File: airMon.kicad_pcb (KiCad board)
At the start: 2 copper layers, 64.8 x 99.7 mm, 120 parts, among them J1 JTAG, J10 I2C_2_2, J11 I2C_2_3_Buffer, J12 I2C_2_4_Buffer, J13 GPS, J14 A3, J15 A4, J16 Rain, J17 GPIO, J18 Wind, J19 USB_B_Micro, J2 PMS7003, J20 Power, J3 PMSx003, J4 SDS011, J5 Conn_01x05, J6 SW, J7 I2C_1_1, J8 I2C_1_2, J9 I2C_2_1, Q1 2N7002NXAK, Q2 BSH202, Q3 SS8050, Q4 SS8050, Q5 2N7002NXAK, Q6 BSH202, Q7 2N7002NXAK, Q8 BSH202, U1 ESP32-WROOM-32, U2 P82B715, U3 L76, U4 PCA9536D, U5 CH340C, U6 LMR14010ADDCR, U7 LMR14010ADDCR

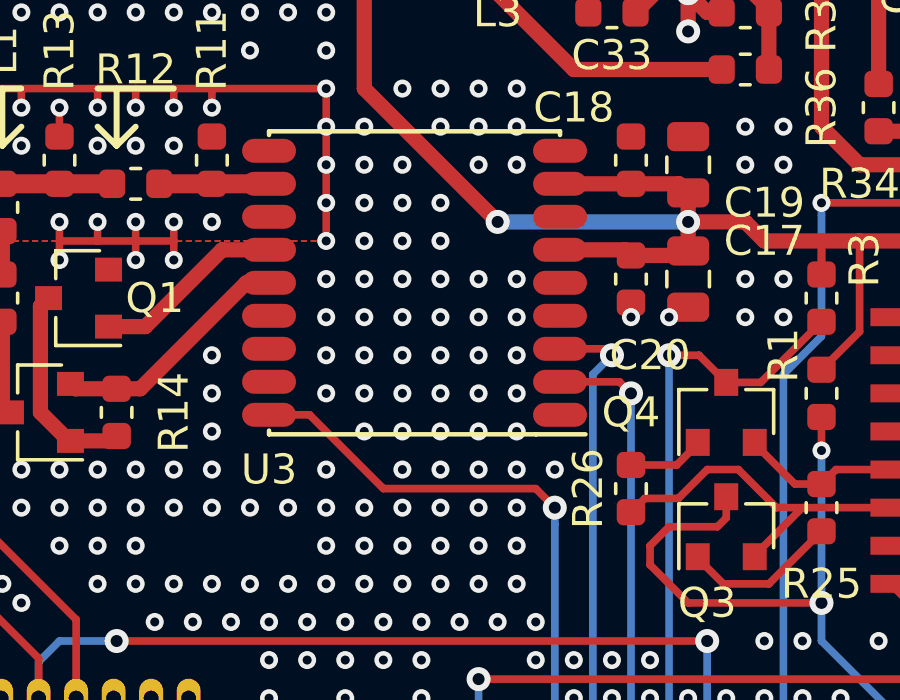
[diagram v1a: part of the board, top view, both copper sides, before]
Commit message: Added Readme Added GNSS receiver list Fixed GNSS receiver connections Improved Pictures
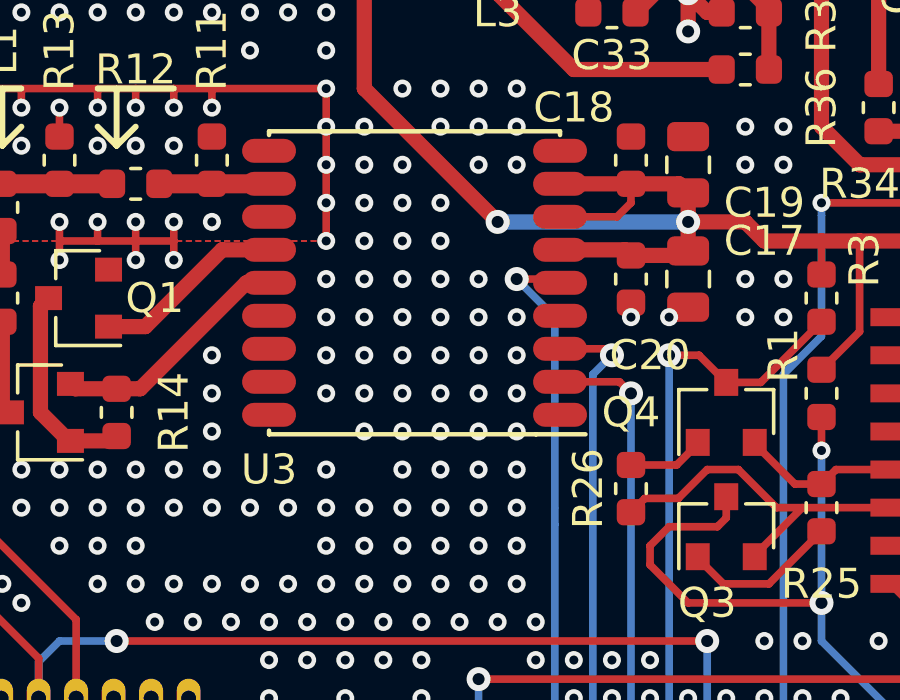
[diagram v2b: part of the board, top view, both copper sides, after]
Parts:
- U3: value L76 -> L70/L76/MAX-M8C/MAX-M8Q/MAX-8C/MAX-8Q
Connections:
- U3 pad 18: /GPS_Wake -> (no net)
- U3 pad 5: (no net) -> /GPS_Wake
- U3 pad 7: (no net) -> VCC
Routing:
- net VCC: track 517.1 -> 520.3 mm
- net /GPS_Wake: track 73.6 -> 72.4 mm
- net VSS: vias 782 -> 780
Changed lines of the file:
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@@
     (thickness 1.6)
     (drawings 71)
-    (tracks 1711)
+    (tracks 1712)
     (zones 0)
     (modules 120)
@@
   )
   (setup
-    (last_trace_width 0.256)
+    (last_trace_width 0.254)
     (user_trace_width 0.127)
     (user_trace_width 0.254)
@@
       (effects (font (size 1 1) (thickness 0.15)))
     )
-    (fp_text value L76 (at 0 0 90) (layer F.Fab)
+    (fp_text value L70/L76/MAX-M8C/MAX-M8Q/MAX-8C/MAX-8Q (at 0 0 90) (layer F.Fab)
       (effects (font (size 1 1) (thickness 0.15)))
     )
@@
     (fp_line (start 5.05 4.85) (end 4.925 4.85) (layer F.SilkS) (width 0.15))
     (fp_line (start 5.05 -4.85) (end 4.925 -4.85) (layer F.SilkS) (width 0.15))
-    (pad 18 smd roundrect (at -4.4 -4.85 90) (size 0.8 1.8) (layers F.Cu F.Paste F.Mask) (roundrect_rratio 0.5)
-      (net 46 /GPS_Wake))
+    (pad 18 smd roundrect (at -4.4 -4.85 90) (size 0.8 1.8) (layers F.Cu F.Paste F.Mask) (roundrect_rratio 0.5))
     (pad 1 smd roundrect (at -4.4 4.85 90) (size 0.8 1.8) (layers F.Cu F.Paste F.Mask) (roundrect_rratio 0.5)
       (net 1 VSS))
@@
     (pad 14 smd roundrect (at 0 -4.85 90) (size 0.8 1.8) (layers F.Cu F.Paste F.Mask) (roundrect_rratio 0.5)
       (net 35 "Net-(Q2-Pad2)"))
-    (pad 5 smd roundrect (at 0 4.85 90) (size 0.8 1.8) (layers F.Cu F.Paste F.Mask) (roundrect_rratio 0.5))
+    (pad 5 smd roundrect (at 0 4.85 90) (size 0.8 1.8) (layers F.Cu F.Paste F.Mask) (roundrect_rratio 0.5)
+      (net 46 /GPS_Wake))
     (pad 13 smd roundrect (at 1.1 -4.85 90) (size 0.8 1.8) (layers F.Cu F.Paste F.Mask) (roundrect_rratio 0.5)
       (net 34 "Net-(Q1-Pad1)"))
@@
     (pad 12 smd roundrect (at 2.2 -4.85 90) (size 0.8 1.8) (layers F.Cu F.Paste F.Mask) (roundrect_rratio 0.5)
       (net 1 VSS))
-    (pad 7 smd roundrect (at 2.2 4.85 90) (size 0.8 1.8) (layers F.Cu F.Paste F.Mask) (roundrect_rratio 0.5))
+    (pad 7 smd roundrect (at 2.2 4.85 90) (size 0.8 1.8) (layers F.Cu F.Paste F.Mask) (roundrect_rratio 0.5)
+      (net 3 VCC))
     (pad 11 smd roundrect (at 3.3 -4.85 90) (size 0.8 1.8) (layers F.Cu F.Paste F.Mask) (roundrect_rratio 0.5)
       (net 41 /GPS/ANT_1))
@@
     )
   )
+  (gr_arc (start 85.09 43.815) (end 83.820001 41.275001) (angle -36.86989765) (layer Edge.Cuts) (width 0.2))
+  (gr_arc (start 85.09 53.975) (end 82.550001 55.244999) (angle -36.86989765) (layer Edge.Cuts) (width 0.2))
   (gr_text "Designed by Jörg Bayer" (at 60.325 21.59) (layer B.SilkS)
     (effects (font (size 1.5 1.5) (thickness 0.3)) (justify mirror))
@@
   (gr_line (start 31.115 38.1) (end 30.48 37.465) (layer F.SilkS) (width 0.2))
   (gr_line (start 31.115 36.195) (end 31.115 38.1) (layer F.SilkS) (width 0.2))
-  (gr_arc (start 85.09 43.815) (end 83.820001 41.275001) (angle -36.86989765) (layer Edge.Cuts) (width 0.2))
   (gr_line (start 82.55 42.545) (end 82.55 55.245) (layer Edge.Cuts) (width 0.2))
-  (gr_arc (start 85.09 53.975) (end 82.550001 55.244999) (angle -36.86989765) (layer Edge.Cuts) (width 0.2))
   (gr_line (start 83.82 56.515) (end 83.82 118.745) (layer Edge.Cuts) (width 0.2))
   (gr_line (start 83.82 41.275) (end 83.82 19.05) (layer Edge.Cuts) (width 0.2))
@@
   (via (at 46.99 42.545) (size 0.6) (drill 0.3) (layers F.Cu B.Cu) (net 1))
   (via (at 48.26 43.815) (size 0.6) (drill 0.3) (layers F.Cu B.Cu) (net 1))
-  (via (at 48.26 42.545) (size 0.6) (drill 0.3) (layers F.Cu B.Cu) (net 1))
   (via (at 44.45 38.735) (size 0.6) (drill 0.3) (layers F.Cu B.Cu) (net 1))
   (via (at 43.18 37.465) (size 0.6) (drill 0.3) (layers F.Cu B.Cu) (net 1))
@@
   (via (at 56.515 102.235) (size 0.6) (drill 0.3) (layers F.Cu B.Cu) (net 1))
   (via (at 55.245 102.235) (size 0.6) (drill 0.3) (layers F.Cu B.Cu) (net 1))
-  (via (at 49.53 48.895) (size 0.6) (drill 0.3) (layers F.Cu B.Cu) (net 1))
   (via (at 52.07 43.815) (size 0.6) (drill 0.3) (layers F.Cu B.Cu) (net 1))
   (via (at 69.215 54.61) (size 0.6) (drill 0.3) (layers F.Cu B.Cu) (net 1))
@@
   (segment (start 76.2 44.45) (end 76.2 54.61) (width 1.27) (layer B.Cu) (net 3))
   (segment (start 76.2 54.61) (end 82.55 60.96) (width 1.27) (layer B.Cu) (net 3))
+  (segment (start 49.705 40.47) (end 51.605 40.47) (width 0.254) (layer F.Cu) (net 3))
+  (segment (start 51.605 40.47) (end 52.07 40.005) (width 0.254) (layer F.Cu) (net 3))
+  (segment (start 52.07 40.005) (end 52.07 39.37) (width 0.254) (layer F.Cu) (net 3))
   (via (at 52.07 102.235) (size 0.8) (drill 0.4) (layers F.Cu B.Cu) (net 4))
   (segment (start 51.504315 102.235) (end 52.07 102.235) (width 0.256) (layer F.Cu) (net 4))
@@
   (via (at 48.26 106.045) (size 0.8) (drill 0.4) (layers F.Cu B.Cu) (net 46))
   (segment (start 42.935 106.045) (end 48.26 106.045) (width 0.256) (layer F.Cu) (net 46))
-  (via (at 49.53 50.165) (size 0.8) (drill 0.4) (layers F.Cu B.Cu) (net 46))
   (segment (start 46.99 67.945) (end 49.53 65.405) (width 0.256) (layer B.Cu) (net 46))
   (segment (start 48.26 106.045) (end 46.99 104.775) (width 0.256) (layer B.Cu) (net 46))
@@
   (segment (start 49.53 65.405) (end 49.53 50.730685) (width 0.256) (layer B.Cu) (net 46))
   (segment (start 46.99 104.775) (end 46.99 67.945) (width 0.256) (layer B.Cu) (net 46))
-  (segment (start 48.895 49.53) (end 49.53 50.165) (width 0.256) (layer F.Cu) (net 46))
-  (segment (start 43.815 49.53) (end 48.895 49.53) (width 0.256) (layer F.Cu) (net 46))
-  (segment (start 40.005 47.07) (end 41.355 47.07) (width 0.256) (layer F.Cu) (net 46))
-  (segment (start 41.355 47.07) (end 43.815 49.53) (width 0.256) (layer F.Cu) (net 46))
+  (via (at 48.26 42.545) (size 0.8) (drill 0.4) (layers F.Cu B.Cu) (net 46))
+  (segment (start 49.53 50.165) (end 49.53 43.815) (width 0.254) (layer B.Cu) (net 46))
+  (segment (start 49.53 43.815) (end 48.26 42.545) (width 0.254) (layer B.Cu) (net 46))
+  (segment (start 49.58 42.545) (end 49.705 42.67) (width 0.254) (layer F.Cu) (net 46))
+  (segment (start 48.26 42.545) (end 49.58 42.545) (width 0.254) (layer F.Cu) (net 46))
   (segment (start 29.975 22.225) (end 29.845 22.095) (width 0.508) (layer F.Cu) (net 47))
   (segment (start 32.385 22.225) (end 29.975 22.225) (width 0.508) (layer F.Cu) (net 47))
